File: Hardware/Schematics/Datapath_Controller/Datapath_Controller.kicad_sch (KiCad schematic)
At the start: 5 parts

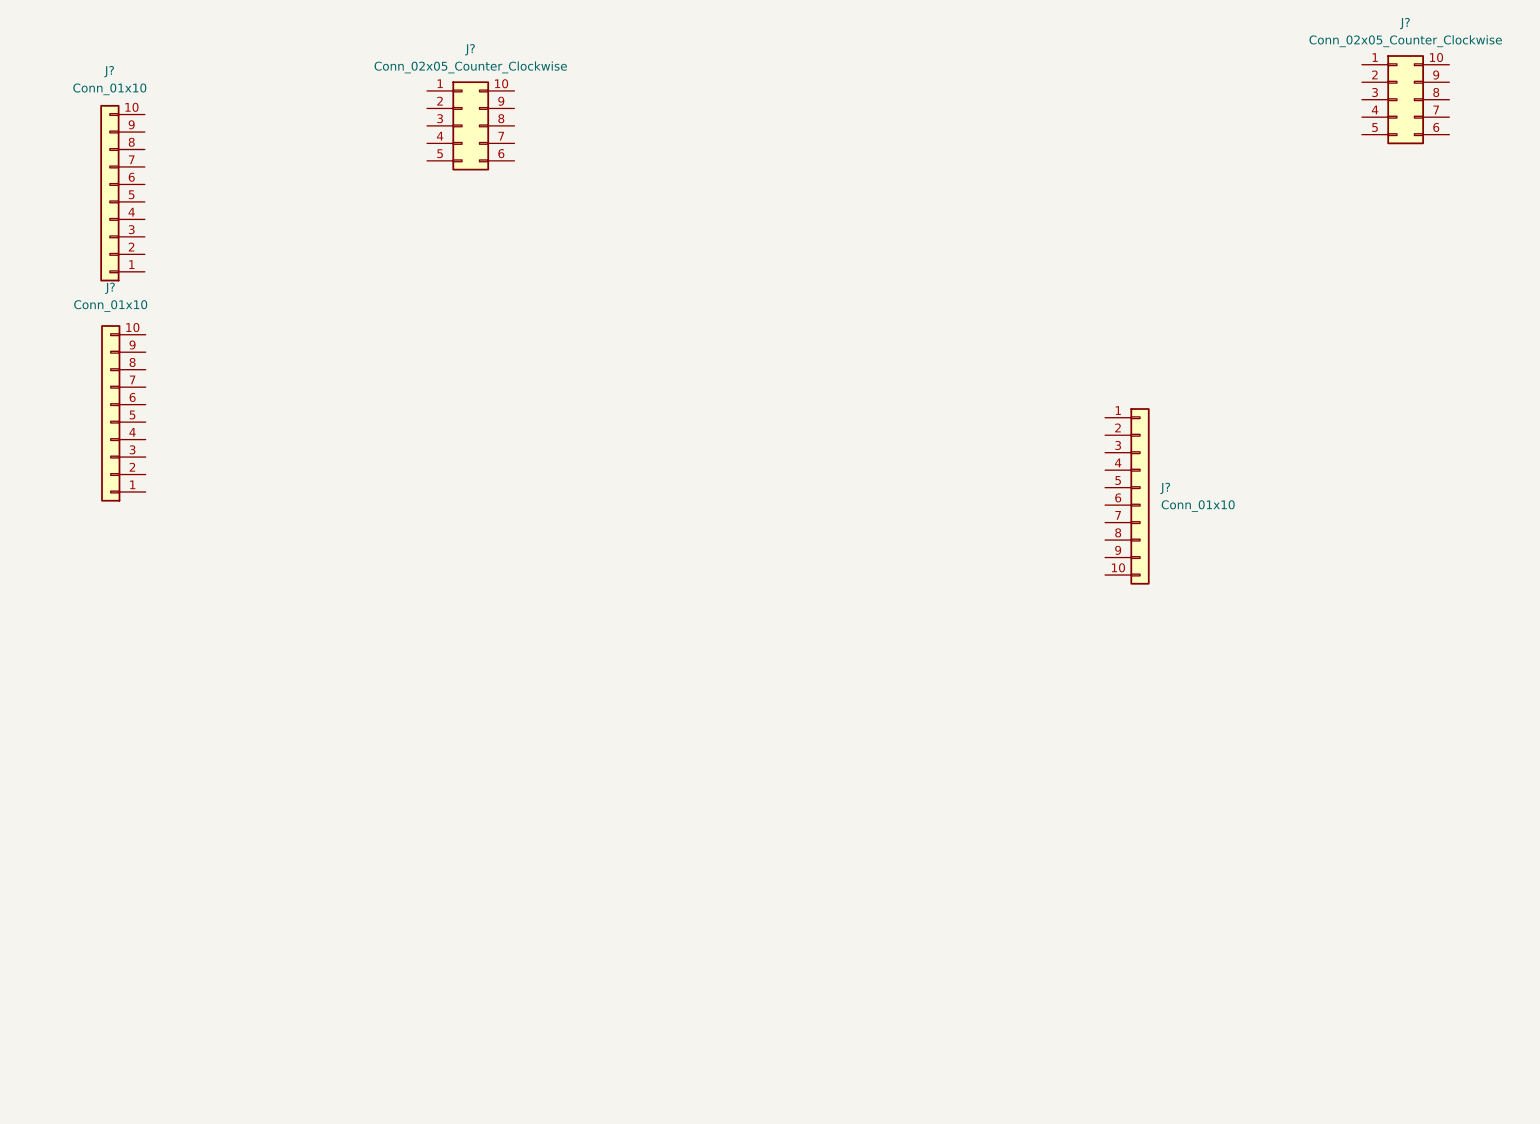
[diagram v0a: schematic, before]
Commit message: Finished Datapath Controller
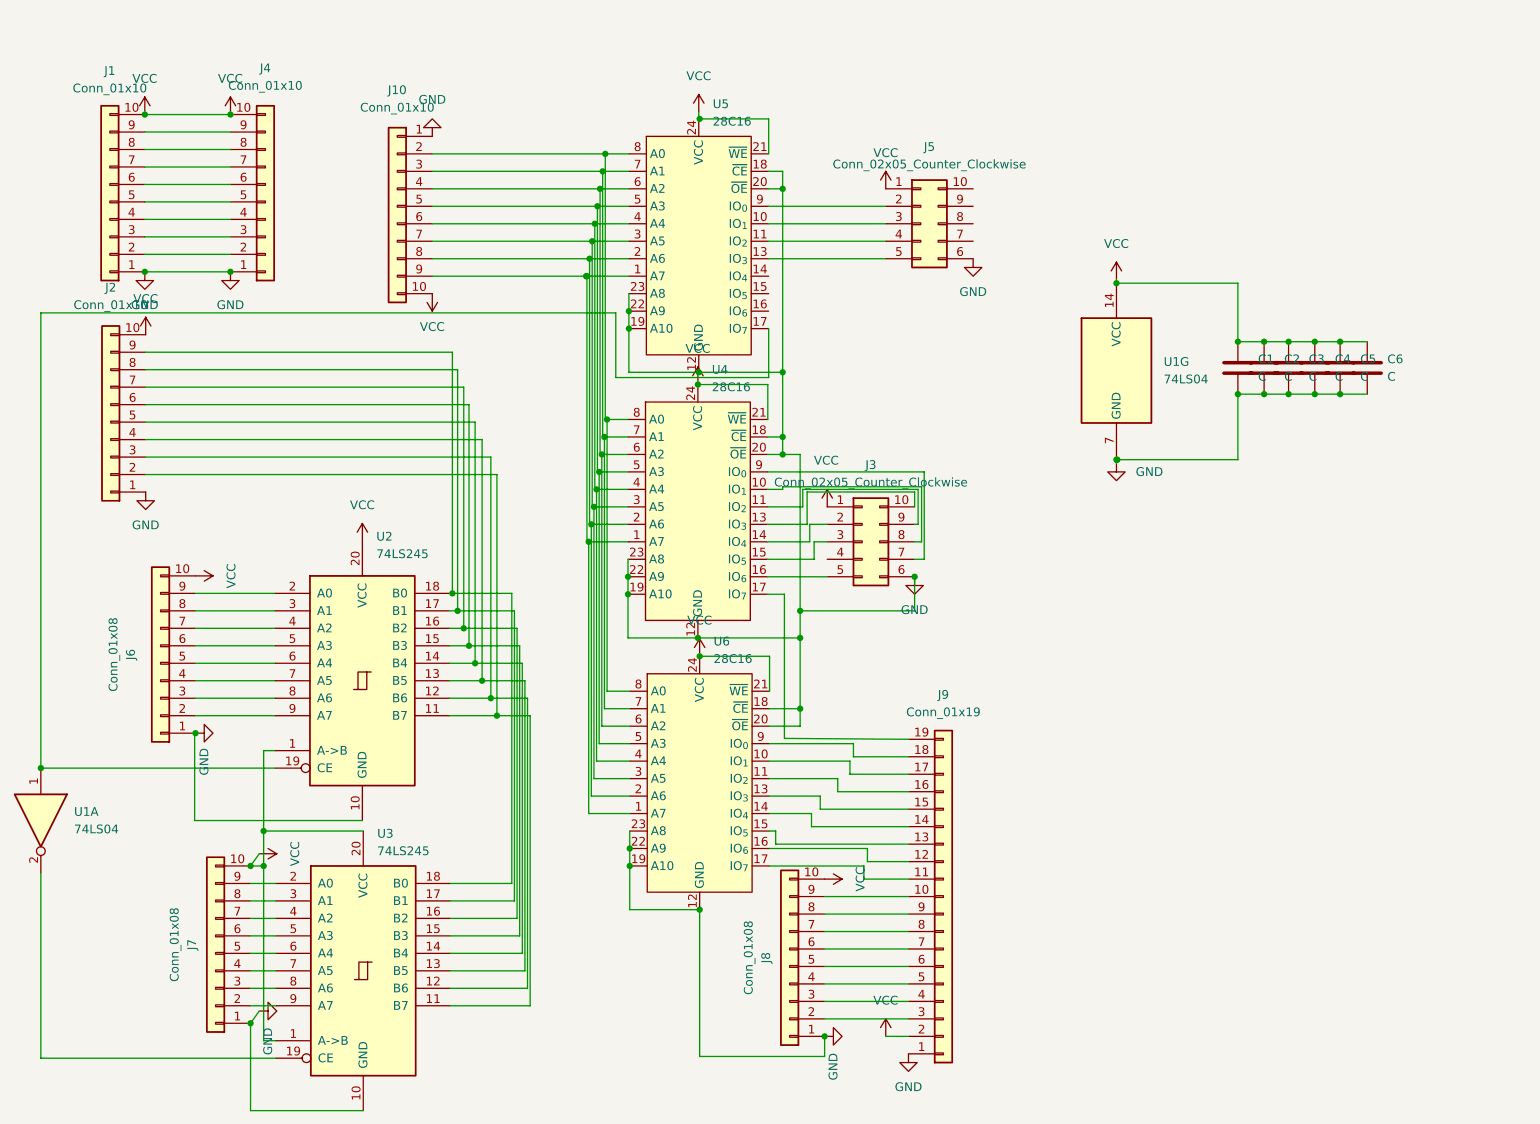
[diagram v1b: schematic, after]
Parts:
- added C1, C2, C3, C4, C5, C6: C, Capacitor_THT:C_Rect_L7.0mm_W2.5mm_P5.00mm, symbol Device:C
- added J10: Conn_01x10, Connector_PinHeader_2.54mm:PinHeader_1x10_P2.54mm_Vertical, symbol Connector_Generic:Conn_01x10
- added J6, J7, J8: Conn_01x08, Connector_PinHeader_2.54mm:PinHeader_1x10_P2.54mm_Vertical, symbol Connector_Generic:Conn_01x10
- added J9: Conn_01x19, Connector_PinHeader_2.54mm:PinHeader_1x19_P2.54mm_Vertical, symbol Connector_Generic:Conn_01x19
- added U1: 74LS04, Package_DIP:DIP-14_W7.62mm_Socket_LongPads, symbol 74xx:74LS04
- added U2, U3: 74LS245, Package_DIP:DIP-20_W7.62mm_Socket_LongPads, symbol 74xx:74LS245
- added U4, U5, U6: 28C16, Package_DIP:DIP-24_W15.24mm_Socket_LongPads, symbol Memory_EPROM:28C16
- J1, J2, J4: renamed from J?; footprint Connector_PinHeader_2.54mm:PinHeader_1x10_P2.54mm_Horizontal -> Connector_PinHeader_2.54mm:PinHeader_1x10_P2.54mm_Vertical
- J3, J5: renamed from J?; footprint Connector_PinHeader_2.54mm:PinHeader_2x05_P2.54mm_Horizontal -> Connector_PinHeader_2.54mm:PinHeader_2x05_P2.54mm_Vertical
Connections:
- net VCC: now reaches J5.1 (Pin_1)
- net VCC: now also J1.10 (Pin_10), J2.10 (Pin_10), J3.1 (Pin_1), J4.10 (Pin_10), C1.1, C2.1, C3.1, C4.1, C5.1, C6.1, J10.10 (Pin_10), J6.10 (Pin_10), J7.10 (Pin_10), J8.10 (Pin_10), J9.2 (Pin_2), U1.14 (VCC), U2.1 (A->B), U2.20 (VCC), U3.1 (A->B), U3.20 (VCC), U4.21 (~{WE}), U4.24 (VCC), U5.24 (VCC), U6.21 (~{WE}), U6.24 (VCC)
- net at J5.2 (Pin_2): now also U5.9 (IO_{0})
- net at J5.3 (Pin_3): now also U5.10 (IO_{1})
- net at J5.4 (Pin_4): now also U5.11 (IO_{2})
- net at J5.5 (Pin_5): now also U5.13 (IO_{3})
- net GND: now reaches J5.6 (Pin_6)
- net GND: now also J1.1 (Pin_1), J2.1 (Pin_1), J3.6 (Pin_6), J4.1 (Pin_1), C1.2, C2.2, C3.2, C4.2, C5.2, C6.2, J10.1 (Pin_1), J6.1 (Pin_1), J7.1 (Pin_1), J8.1 (Pin_1), J9.1 (Pin_1), U1.7 (GND), U2.10 (GND), U3.10 (GND), U4.12 (GND), U4.18 (~{CE}), U4.19 (A10), U4.20 (~{OE}), U4.22 (A9), U4.23 (A8), U5.12 (GND), U5.18 (~{CE}), U5.19 (A10), U5.20 (~{OE}), U5.22 (A9), U5.23 (A8), U6.12 (GND), U6.18 (~{CE}), U6.19 (A10), U6.20 (~{OE}), U6.22 (A9), U6.23 (A8)
- net at J2.2 (Pin_2): now also U2.11 (B7), U3.11 (B7)
- net at J2.3 (Pin_3): now also U2.12 (B6), U3.12 (B6)
- net at J2.4 (Pin_4): now also U2.13 (B5), U3.13 (B5)
- net at J2.5 (Pin_5): now also U2.14 (B4), U3.14 (B4)
- net at J2.6 (Pin_6): now also U2.15 (B3), U3.15 (B3)
- net at J2.7 (Pin_7): now also U2.16 (B2), U3.16 (B2)
- net at J2.8 (Pin_8): now also U2.17 (B1), U3.17 (B1)
- net at J2.9 (Pin_9): now also U2.18 (B0), U3.18 (B0)
- net at J4.2 (Pin_2): now also J1.2 (Pin_2)
- net at J4.3 (Pin_3): now also J1.3 (Pin_3)
- net at J4.4 (Pin_4): now also J1.4 (Pin_4)
- net at J4.5 (Pin_5): now also J1.5 (Pin_5)
- net at J4.6 (Pin_6): now also J1.6 (Pin_6)
- net at J4.7 (Pin_7): now also J1.7 (Pin_7)
- net at J4.8 (Pin_8): now also J1.8 (Pin_8)
- net at J4.9 (Pin_9): now also J1.9 (Pin_9)
- net at J3.10 (Pin_10): now also U4.13 (IO_{3})
- net at J3.2 (Pin_2): now also U4.14 (IO_{4})
- net at J3.3 (Pin_3): now also U4.15 (IO_{5})
- net at J3.5 (Pin_5): now also U4.16 (IO_{6})
- net at J3.7 (Pin_7): now also U4.9 (IO_{0})
- net at J3.8 (Pin_8): now also U4.10 (IO_{1})
- net at J3.9 (Pin_9): now also U4.11 (IO_{2})
- new net: J10.9 (Pin_9), U4.1 (A7), U5.1 (A7), U6.1 (A7)
- new net: J9.17 (Pin_17), U6.10 (IO_{1})
- new net: J9.16 (Pin_16), U6.11 (IO_{2})
- new net: J9.15 (Pin_15), U6.13 (IO_{3})
- new net: J9.14 (Pin_14), U6.14 (IO_{4})
- new net: J9.13 (Pin_13), U6.15 (IO_{5})
- new net: J9.12 (Pin_12), U6.16 (IO_{6})
- new net: J9.11 (Pin_11), U6.17 (IO_{7})
- new net: J10.8 (Pin_8), U4.2 (A6), U5.2 (A6), U6.2 (A6)
- new net: J10.7 (Pin_7), U4.3 (A5), U5.3 (A5), U6.3 (A5)
- new net: J10.6 (Pin_6), U4.4 (A4), U5.4 (A4), U6.4 (A4)
- new net: J10.5 (Pin_5), U4.5 (A3), U5.5 (A3), U6.5 (A3)
- new net: J10.4 (Pin_4), U4.6 (A2), U5.6 (A2), U6.6 (A2)
- new net: J10.3 (Pin_3), U4.7 (A1), U5.7 (A1), U6.7 (A1)
- new net: J10.2 (Pin_2), U4.8 (A0), U5.8 (A0), U6.8 (A0)
- new net: J9.18 (Pin_18), U6.9 (IO_{0})
- new net: J8.2 (Pin_2), J9.3 (Pin_3)
- new net: J8.3 (Pin_3), J9.4 (Pin_4)
- new net: J8.4 (Pin_4), J9.5 (Pin_5)
- new net: J8.5 (Pin_5), J9.6 (Pin_6)
- new net: J8.6 (Pin_6), J9.7 (Pin_7)
- new net: J8.7 (Pin_7), J9.8 (Pin_8)
- new net: J8.8 (Pin_8), J9.9 (Pin_9)
- new net: J8.9 (Pin_9), J9.10 (Pin_10)
- new net: U1.1, U2.19 (CE), U5.17 (IO_{7})
- new net: J6.9 (Pin_9), U2.2 (A0)
- new net: J6.8 (Pin_8), U2.3 (A1)
- new net: J6.7 (Pin_7), U2.4 (A2)
- new net: J6.6 (Pin_6), U2.5 (A3)
- new net: J6.5 (Pin_5), U2.6 (A4)
- new net: J6.4 (Pin_4), U2.7 (A5)
- new net: J6.3 (Pin_3), U2.8 (A6)
- new net: J6.2 (Pin_2), U2.9 (A7)
- new net: U1.2, U3.19 (CE)
- new net: J7.9 (Pin_9), U3.2 (A0)
- new net: J7.8 (Pin_8), U3.3 (A1)
- new net: J7.7 (Pin_7), U3.4 (A2)
- new net: J7.6 (Pin_6), U3.5 (A3)
- new net: J7.5 (Pin_5), U3.6 (A4)
- new net: J7.4 (Pin_4), U3.7 (A5)
- new net: J7.3 (Pin_3), U3.8 (A6)
- new net: J7.2 (Pin_2), U3.9 (A7)
- new net: J9.19 (Pin_19), U4.17 (IO_{7})
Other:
- moved on the sheet: J3, J4, J5
